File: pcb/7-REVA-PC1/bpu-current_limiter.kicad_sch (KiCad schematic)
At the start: 47 parts, among them Q401 BCM857, Q402 BC2301T 2.8A, Q601 MMDT3906, Q602 BC2301T 2.8A, U601 GS321A-TR, U602 GSV331-TR, U603 LMV321

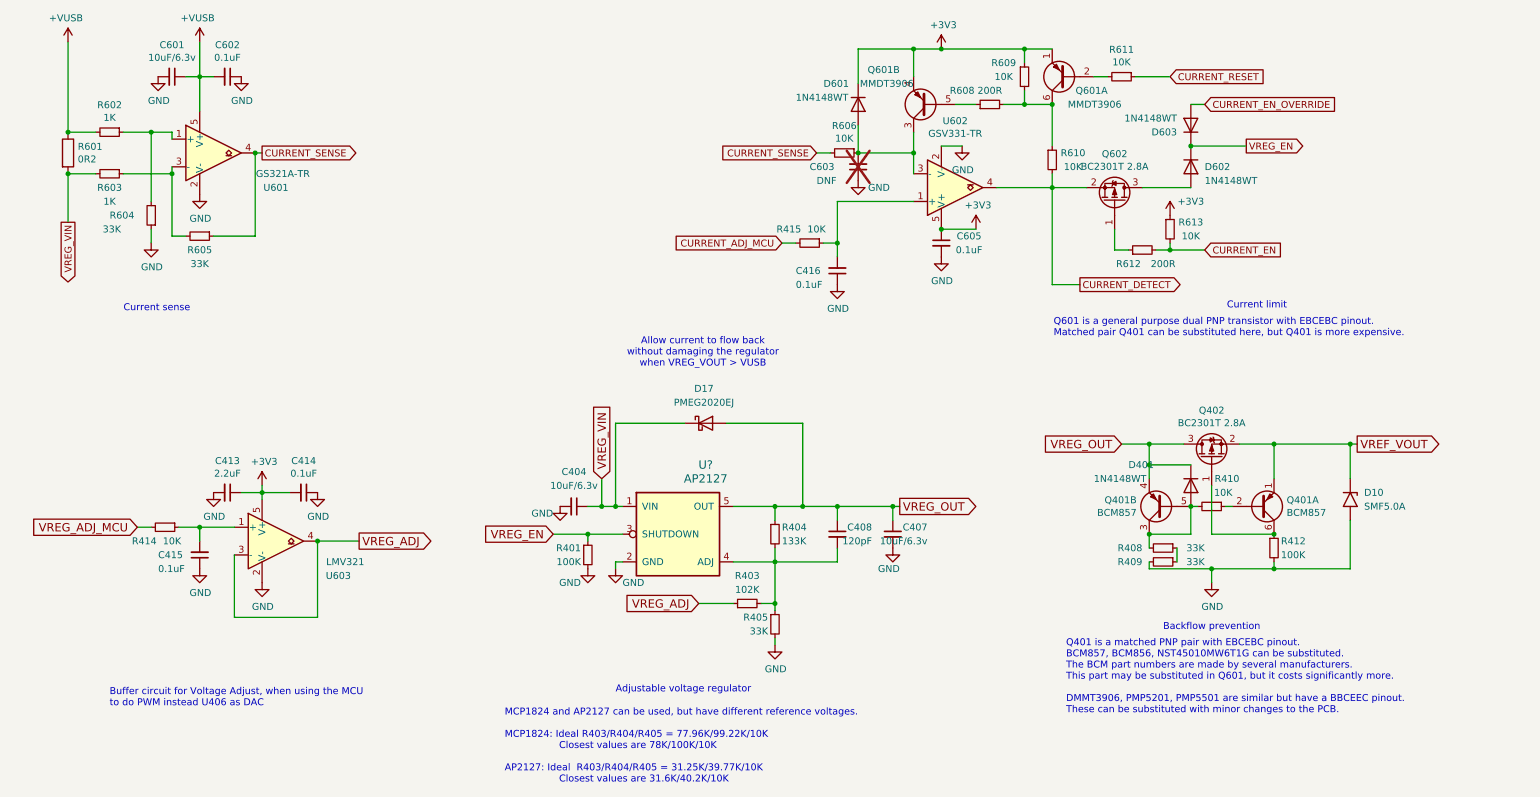
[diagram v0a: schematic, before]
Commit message: Remove DNF footprints, locate PWM pins for power supply adjustment. Change PWM op-amp to DFN and buffer also the CURRENT_ADJ. Remove a FET gate resistor from current limiter.
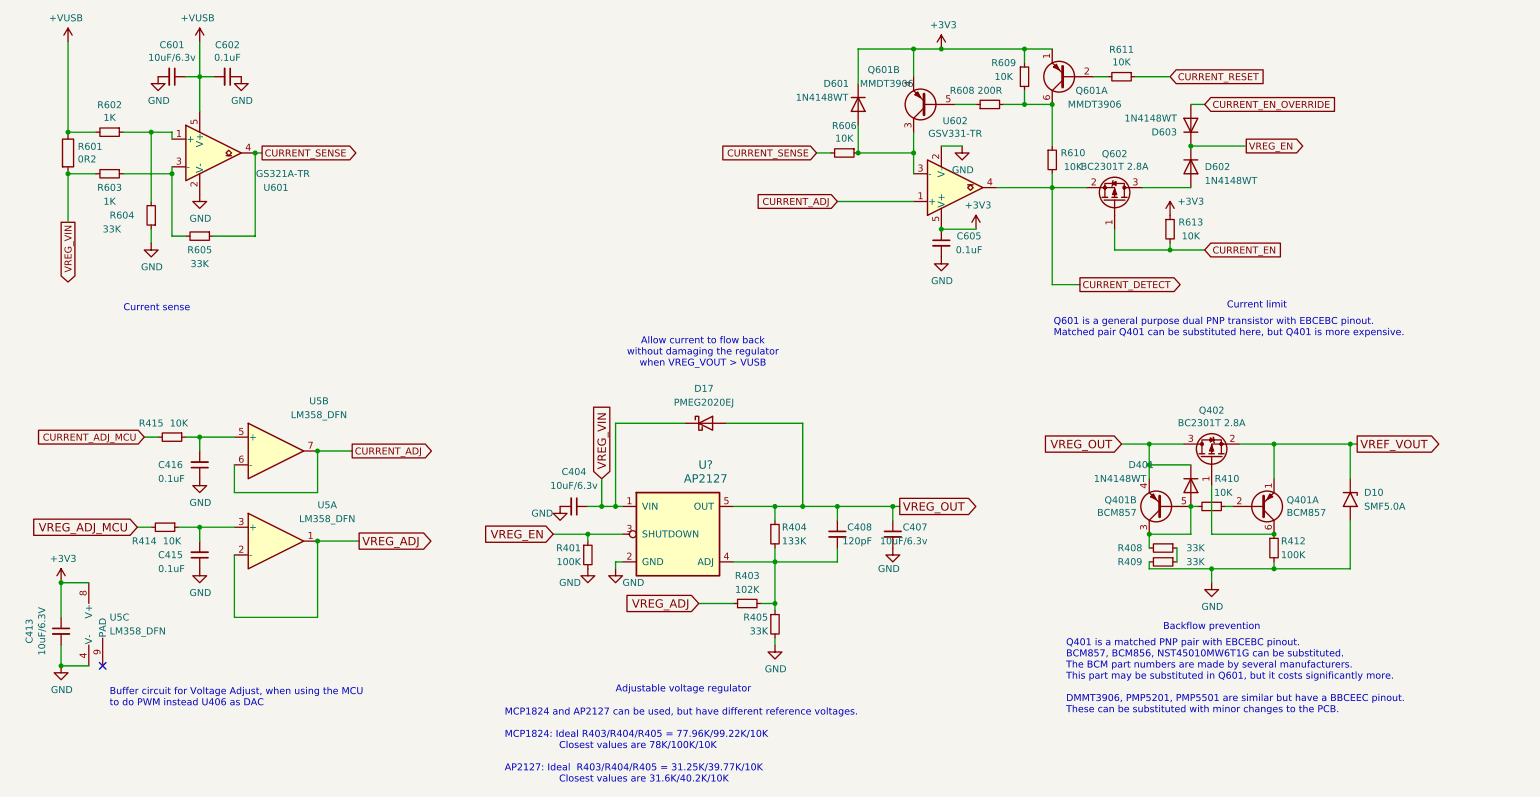
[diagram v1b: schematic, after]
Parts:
- removed C414: 0.1uF, Capacitor_SMD:C_0402_1005Metric, symbol Device:C_Small
- removed C603: DNF, Capacitor_SMD:C_0402_1005Metric, symbol Device:C_Small
- removed R612: 200R, Resistor_SMD:R_0402_1005Metric, symbol Device:R_Small
- removed U603: LMV321, Package_TO_SOT_SMD:SOT-23-5, symbol Comparator:LMV331
- added U5: LM358_DFN, Package_DFN_QFN:DFN-8-1EP_2x2mm_P0.5mm_EP1.05x1.75mm, symbol Amplifier_Operational:LM358_DFN
- C413: value 2.2uF -> 10uF/6.3V
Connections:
- net +3V3: now also U5.8 (V+)
- net CURRENT_EN: now also Q602.1 (G)
- net GND: now also U5.4 (V-)
- net VREG_ADJ: now also U5.1, U5.2 (-)
- net at C416.2, R415.1: now also U5.5 (+); no longer U602.1 (+)
- net at C415.2, R414.1: now also U5.3 (+)
- new net CURRENT_ADJ: U5.6 (-), U5.7, U602.1 (+)
- no-connect marks 0 -> 1
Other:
- moved on the sheet: C413, C416, R415

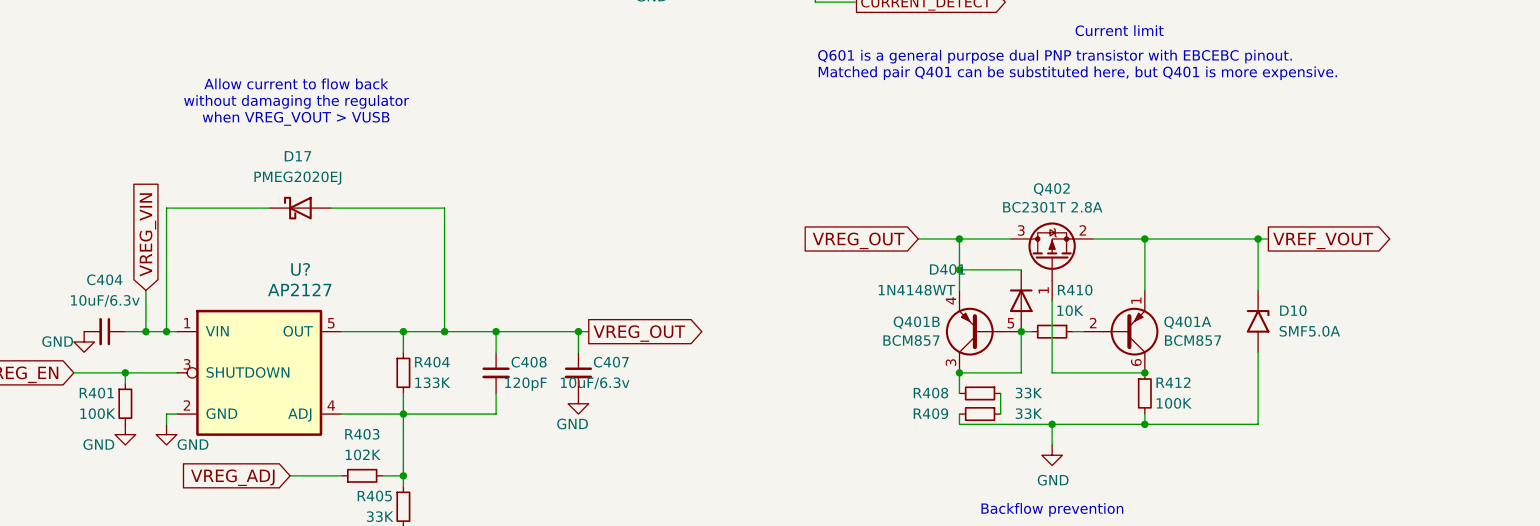
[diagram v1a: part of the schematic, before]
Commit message: Remove VREG bypass diode. Fix XL9555 I2C address
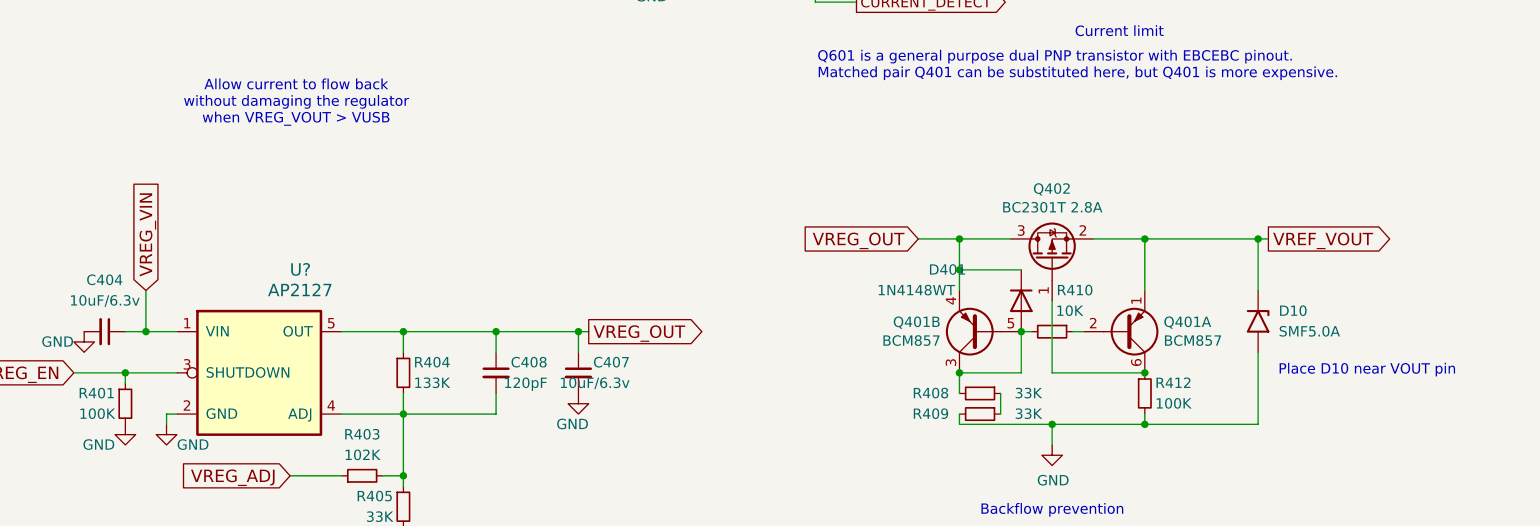
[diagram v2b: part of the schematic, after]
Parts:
- removed D17: PMEG2020EJ, Diode_SMD:D_SOD-323F, symbol Device:D_Schottky
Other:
- note added: "Place D10 near VOUT pin"
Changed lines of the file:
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@@
 	)
 	(junction
-		(at 156.21 106.68)
-		(diameter 0)
-		(color 0 0 0 0)
-	)
-	(junction
 		(at 201.93 33.02)
 		(diameter 0)
@@
 	)
 	(junction
-		(at 121.92 106.68)
-		(diameter 0)
-		(color 0 0 0 0)
-	)
-	(junction
 		(at 151.13 116.84)
 		(diameter 0)
@@
 	(wire
 		(pts
-			(xy 156.21 106.68) (xy 162.56 106.68)
-		)
-		(stroke
-			(width 0)
-			(type default)
-		)
-	)
-	(wire
-		(pts
 			(xy 40.64 57.15) (xy 40.64 45.72)
 		)
@@
 	(wire
 		(pts
-			(xy 119.38 106.68) (xy 121.92 106.68)
-		)
-		(stroke
-			(width 0)
-			(type default)
-		)
-	)
-	(wire
-		(pts
 			(xy 256.54 95.25) (xy 257.81 95.25)
 		)
@@
 	(wire
 		(pts
-			(xy 151.13 106.68) (xy 156.21 106.68)
+			(xy 151.13 106.68) (xy 162.56 106.68)
 		)
 		(stroke
@@
 	(wire
 		(pts
-			(xy 156.21 91.44) (xy 156.21 106.68)
-		)
-		(stroke
-			(width 0)
-			(type default)
-		)
-	)
-	(wire
-		(pts
 			(xy 214.63 95.25) (xy 219.71 95.25)
 		)
@@
 	(wire
 		(pts
-			(xy 121.92 91.44) (xy 121.92 106.68)
-		)
-		(stroke
-			(width 0)
-			(type default)
-		)
-	)
-	(wire
-		(pts
 			(xy 212.09 27.94) (xy 209.55 27.94)
 		)
@@
 	(wire
 		(pts
-			(xy 134.62 91.44) (xy 121.92 91.44)
-		)
-		(stroke
-			(width 0)
-			(type default)
-		)
-	)
-	(wire
-		(pts
 			(xy 224.79 114.3) (xy 224.79 116.84)
 		)
@@
 	(wire
 		(pts
-			(xy 121.92 106.68) (xy 123.19 106.68)
+			(xy 119.38 106.68) (xy 123.19 106.68)
 		)
 		(stroke
@@
 	(wire
 		(pts
-			(xy 142.24 91.44) (xy 156.21 91.44)
-		)
-		(stroke
-			(width 0)
-			(type default)
-		)
-	)
-	(wire
-		(pts
 			(xy 45.72 27.94) (xy 48.26 27.94)
 		)
@@
 		)
 	)
+	(text "Place D10 near VOUT pin"
+		(exclude_from_sim no)
+		(at 270.002 111.506 0)
+		(effects
+			(font
+				(size 1.27 1.27)
+			)
+		)
+	)
 	(text "Allow current to flow back\nwithout damaging the regulator\nwhen VREG_VOUT > VUSB"
 		(exclude_from_sim no)
@@
 					(unit 1)
 				)
-			)
-		)
-	)
-	(symbol
-		(lib_id "Device:D_Schottky")
-		(at 138.43 91.44 0)
-		(unit 1)
-		(exclude_from_sim no)
-		(in_bom yes)
-		(on_board yes)
-		(dnp no)
-		(fields_autoplaced yes)
-		(property "Reference" "D17"
-			(at 138.1125 85.09 0)
-			(effects
-				(font
-					(size 1.27 1.27)
-				)
-			)
-		)
-		(property "Value" "PMEG2020EJ"
-			(at 138.1125 87.63 0)
-			(effects
-				(font
-					(size 1.27 1.27)
-				)
-			)
-		)
-		(property "Footprint" "Diode_SMD:D_SOD-323F"
-			(at 138.43 91.44 0)
-			(effects
-				(font
-					(size 1.27 1.27)
-				)
-				(hide yes)
-			)
-		)
-		(property "Datasheet" "https://assets.nexperia.com/documents/data-sheet/PMEG2020EJ.pdf"
-			(at 138.43 91.44 0)
-			(effects
-				(font
-					(size 1.27 1.27)
-				)
-				(hide yes)
-			)
-		)
-		(property "Description" "Schottky diode, 20V, 2A"
-			(at 138.43 91.44 0)
-			(effects
-				(font
-					(size 1.27 1.27)
-				)
-				(hide yes)
-			)
-		)
-		(property "Description_1" ""
-			(at 138.43 91.44 0)
-			(effects
-				(font
-					(size 1.27 1.27)
-				)
-				(hide yes)
-			)
-		)
-		(property "MANUFACTURER" "Nexperia"
-			(at 138.43 91.44 0)
-			(effects
-				(font
-					(size 1.27 1.27)
-				)
-				(hide yes)
-			)
-		)
-		(property "MAXIMUM_PACKAGE_HEIGHT" ""
-			(at 138.43 91.44 0)
-			(effects
-				(font
-					(size 1.27 1.27)
-				)
-				(hide yes)
-			)
-		)
-		(property "PARTREV" ""
-			(at 138.43 91.44 0)
-			(effects
-				(font
-					(size 1.27 1.27)
-				)
-				(hide yes)
-			)
-		)
-		(property "STANDARD" ""
-			(at 138.43 91.44 0)
-			(effects
-				(font
-					(size 1.27 1.27)
-				)
-				(hide yes)
-			)
-		)
-		(pin "2"
-		)
-		(pin "1"
-		)
-		(instances
-			(project "7-REV1"
-				(path "/1f56410a-eaac-4444-b0f7-cfd3531e22ac/00000000-0000-0000-0000-00005f46fad3"
-					(reference "D17")
-					(unit 1)
-				)

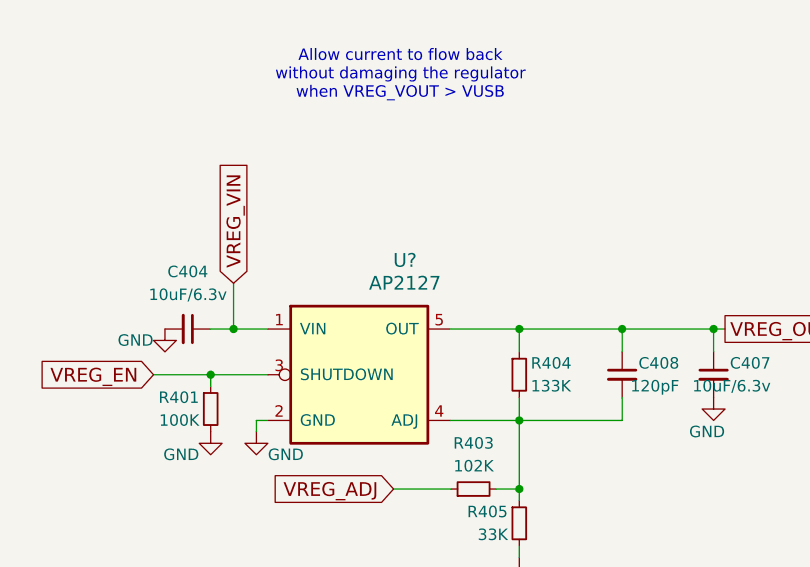
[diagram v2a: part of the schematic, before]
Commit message: Change XL9555 I2C address to advance from TCA6416ARTWR. Change adjustable voltage regulator to correct part number.
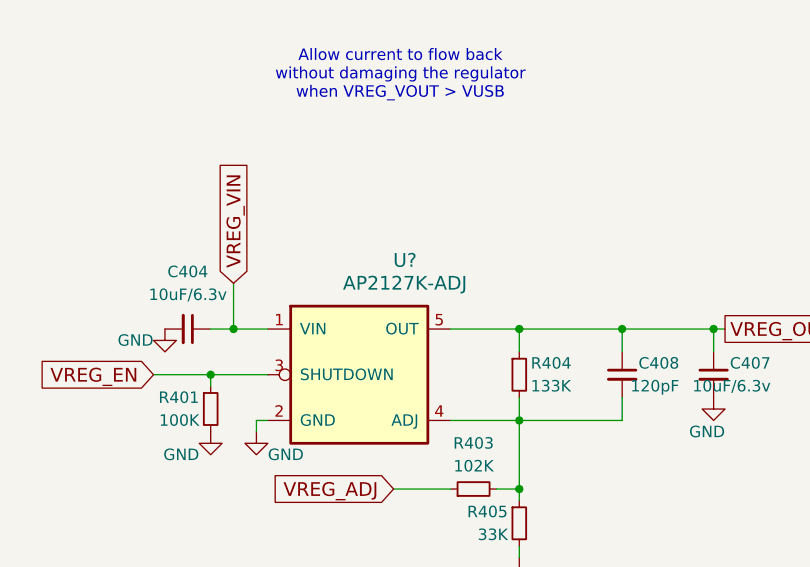
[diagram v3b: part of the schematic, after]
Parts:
- U?: value AP2127 -> AP2127K-ADJ
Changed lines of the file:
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@@
 			)
 		)
-		(property "Value" "AP2127"
+		(property "Value" "AP2127K-ADJ"
 			(at 138.43 101.6 0)
 			(effects

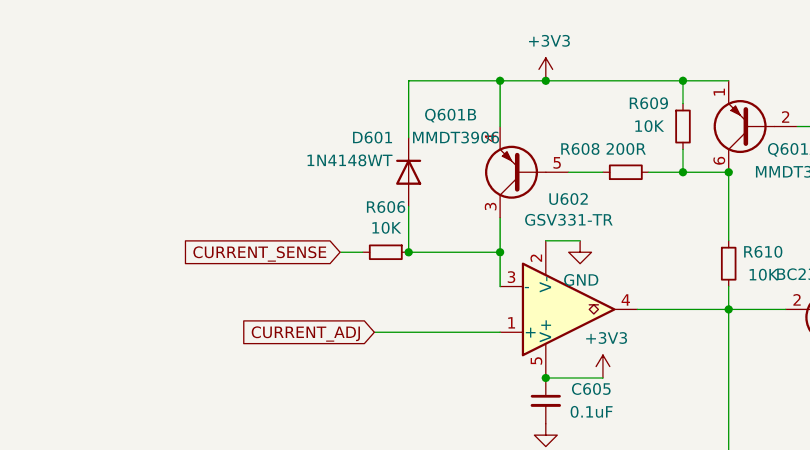
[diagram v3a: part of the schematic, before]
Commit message: remvoe 1n4148 from current fuse
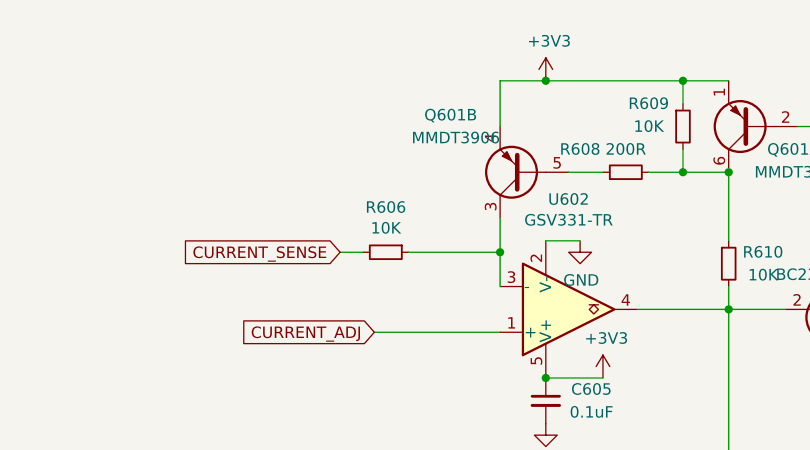
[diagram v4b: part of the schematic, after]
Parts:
- removed D601: 1N4148WT, Diode_SMD:D_SOD-523, symbol Diode:1N4148WS
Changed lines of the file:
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@@
 	)
 	(junction
-		(at 166.37 41.91)
-		(diameter 0)
-		(color 0 0 0 0)
-	)
-	(junction
 		(at 116.84 111.76)
 		(diameter 0)
@@
 	)
 	(junction
-		(at 176.53 22.86)
-		(diameter 0)
-		(color 0 0 0 0)
-	)
-	(junction
 		(at 196.85 33.02)
 		(diameter 0)
@@
 	(wire
 		(pts
-			(xy 166.37 22.86) (xy 166.37 29.21)
-		)
-		(stroke
-			(width 0)
-			(type default)
-		)
-	)
-	(wire
-		(pts
 			(xy 172.72 106.68) (xy 173.99 106.68)
 		)
@@
 	(wire
 		(pts
-			(xy 176.53 22.86) (xy 166.37 22.86)
-		)
-		(stroke
-			(width 0)
-			(type default)
-		)
-	)
-	(wire
-		(pts
 			(xy 201.93 48.26) (xy 201.93 45.72)
 		)
@@
 	(wire
 		(pts
-			(xy 166.37 36.83) (xy 166.37 41.91)
-		)
-		(stroke
-			(width 0)
-			(type default)
-		)
-	)
-	(wire
-		(pts
 			(xy 52.07 115.57) (xy 52.07 127)
 		)
@@
 					(unit 1)
 				)
-			)
-		)
-	)
-	(symbol
-		(lib_id "Diode:1N4148WS")
-		(at 166.37 33.02 270)
-		(unit 1)
-		(exclude_from_sim no)
-		(in_bom yes)
-		(on_board yes)
-		(dnp no)
-		(property "Reference" "D601"
-			(at 160.02 29.21 90)
-			(effects
-				(font
-					(size 1.27 1.27)
-				)
-				(justify left)
-			)
-		)
-		(property "Value" "1N4148WT"
-			(at 154.94 31.75 90)
-			(effects
-				(font
-					(size 1.27 1.27)
-				)
-				(justify left)
-			)
-		)
-		(property "Footprint" "Diode_SMD:D_SOD-523"
-			(at 161.925 33.02 0)
-			(effects
-				(font
-					(size 1.27 1.27)
-				)
-				(hide yes)
-			)
-		)
-		(property "Datasheet" "https://www.vishay.com/docs/85751/1n4148ws.pdf"
-			(at 166.37 33.02 0)
-			(effects
-				(font
-					(size 1.27 1.27)
-				)
-				(hide yes)
-			)
-		)
-		(property "Description" ""
-			(at 166.37 33.02 0)
-			(effects
-				(font
-					(size 1.27 1.27)
-				)
-				(hide yes)
-			)
-		)
-		(property "RMB" "0.182079"
-			(at 166.37 33.02 0)
-			(effects
-				(font
-					(size 1.27 1.27)
-				)
-				(hide yes)
-			)
-		)
-		(property "Supplier" "https://item.szlcsc.com/120141.html"
-			(at 166.37 33.02 0)
-			(effects
-				(font
-					(size 1.27 1.27)
-				)
-				(hide yes)
-			)
-		)
-		(property "Description_1" ""
-			(at 166.37 33.02 0)
-			(effects
-				(font
-					(size 1.27 1.27)
-				)
-				(hide yes)
-			)
-		)
-		(property "MAXIMUM_PACKAGE_HEIGHT" ""
-			(at 166.37 33.02 0)
-			(effects
-				(font
-					(size 1.27 1.27)
-				)
-				(hide yes)
-			)
-		)
-		(property "PARTREV" ""
-			(at 166.37 33.02 0)
-			(effects
-				(font
-					(size 1.27 1.27)
-				)
-				(hide yes)
-			)
-		)
-		(property "STANDARD" ""
-			(at 166.37 33.02 0)
-			(effects
-				(font
-					(size 1.27 1.27)
-				)
-				(hide yes)
-			)
-		)
-		(pin "1"
-		)
-		(pin "2"
-		)
-		(instances
-			(project "REV0"
-				(path "/1f56410a-eaac-4444-b0f7-cfd3531e22ac/00000000-0000-0000-0000-00005f46fad3"
-					(reference "D601")
-					(unit 1)
-				)

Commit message: 7R1 PCB routed
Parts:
- Q402, Q602: footprint Package_TO_SOT_SMD:SOT-523 -> library:SOT-523
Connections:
- net GND: now also U5.9 (PAD)
- no-connect marks 1 -> 0
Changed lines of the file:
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@@
 		(color 0 0 0 0)
 	)
-	(no_connect
-		(at 27.94 135.89)
-	)
 	(wire
 		(pts
@@
 	(text "Buffer circuit for Voltage Adjust, when using the MCU\nto do PWM instead U406 as DAC"
 		(exclude_from_sim no)
-		(at 29.21 143.51 0)
+		(at 26.67 151.13 0)
 		(effects
 			(font
@@
 			)
 		)
-		(property "Footprint" "Package_TO_SOT_SMD:SOT-523"
+		(property "Footprint" "library:SOT-523"
 			(at 211.455 45.72 0)
 			(effects
@@
 			)
 		)
-		(property "Footprint" "Package_TO_SOT_SMD:SOT-523"
+		(property "Footprint" "library:SOT-523"
 			(at 233.045 92.71 0)
 			(effects
@@
 					(unit 1)
 				)
+			)
+		)
+	)
+	(symbol
+		(lib_id "power:GND")
+		(at 27.94 135.89 0)
+		(unit 1)
+		(exclude_from_sim no)
+		(in_bom yes)
+		(on_board yes)
+		(dnp no)
+		(property "Reference" "#PWR094"
+			(at 27.94 142.24 0)
+			(effects
+				(font
+					(size 1.27 1.27)
+				)
+				(hide yes)
+			)
+		)
+		(property "Value" "GND"
+			(at 28.067 140.2842 0)
+			(effects
+				(font
+					(size 1.27 1.27)
+				)
+			)
+		)
+		(property "Footprint" ""
+			(at 27.94 135.89 0)
+			(effects
+				(font
+					(size 1.27 1.27)
+				)
+				(hide yes)
+			)
+		)
+		(property "Datasheet" ""
+			(at 27.94 135.89 0)
+			(effects
+				(font
+					(size 1.27 1.27)
+				)
+				(hide yes)
+			)
+		)
+		(property "Description" ""
+			(at 27.94 135.89 0)
+			(effects
+				(font
+					(size 1.27 1.27)
+				)
+				(hide yes)
+			)
+		)
+		(pin "1"
+		)
+		(instances
+			(project "7-REVA-PC1"
+				(path "/1f56410a-eaac-4444-b0f7-cfd3531e22ac/00000000-0000-0000-0000-00005f46fad3"
+					(reference "#PWR094")
+					(unit 1)
+				)
